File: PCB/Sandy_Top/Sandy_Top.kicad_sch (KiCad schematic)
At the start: 71 parts, among them J1 Conn_02x02_Top_Bottom, J2 Conn_02x02_Top_Bottom, J3 Conn_02x02_Top_Bottom

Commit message: WIP ネジ穴位置、スイッチ位置調整中
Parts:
- added H10, H9: MountingHole, locallib:MountingHole_2.2mm_M2_Pad_minimal, symbol Mechanical:MountingHole_Pad
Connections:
- net Top_GND: now also H10.1, H9.1
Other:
- note added: "Mid to Top: require 12 pins ( = 4 row + 7 col + GND )"
- note added: "ネジ穴をあと2本増やして12本にすれば、ネジ穴導通できる。"
- note removed: "Mid to Top: require 12 pins"
- moved on the sheet: H1, H2, H5, H6, H7, H8

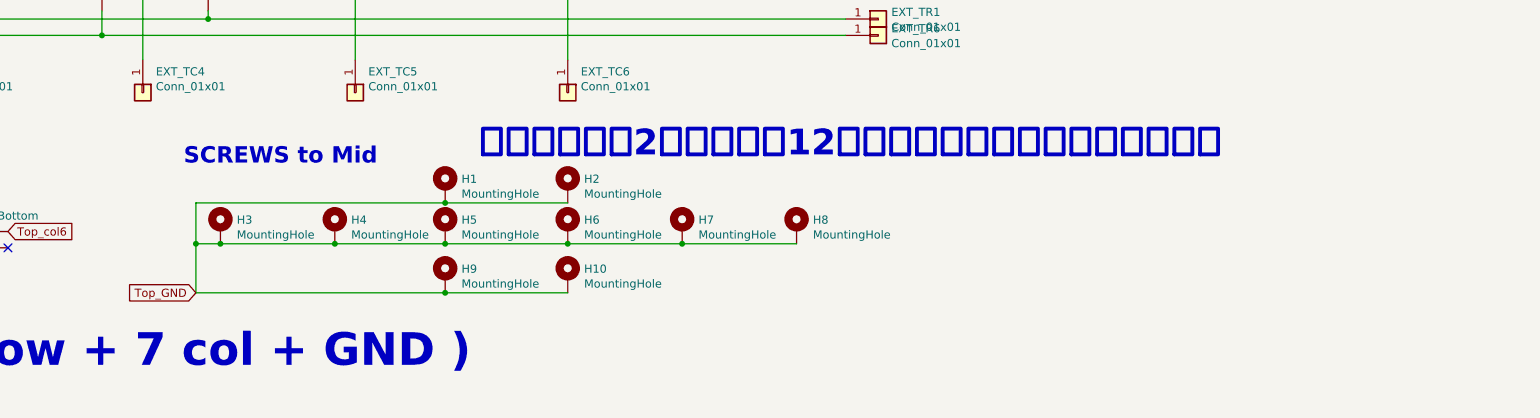
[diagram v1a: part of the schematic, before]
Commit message: Topネジ穴を仮配置
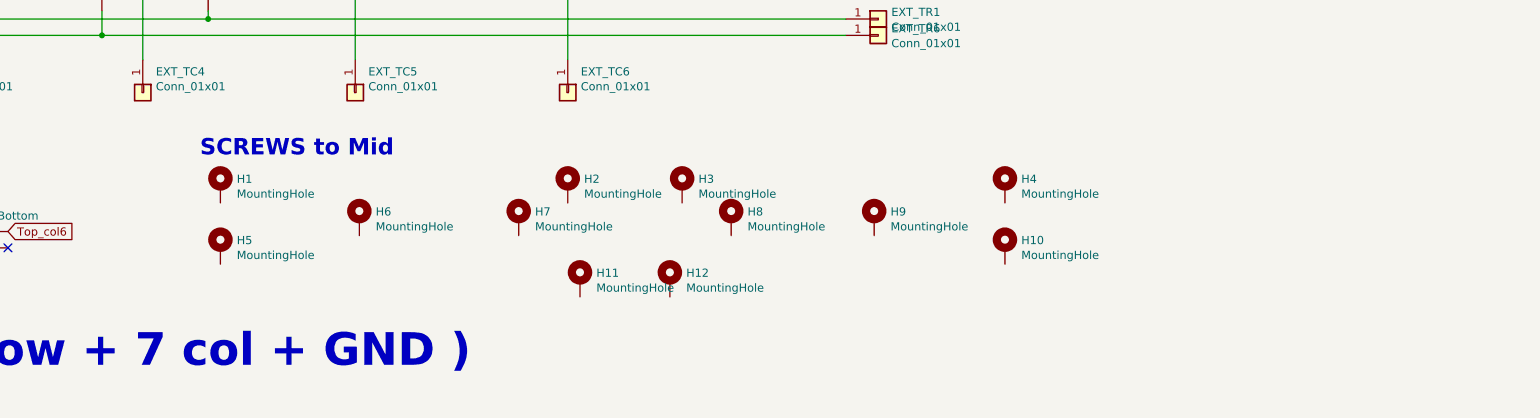
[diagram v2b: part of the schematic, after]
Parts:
- added H11, H12: MountingHole, locallib:MountingHole_2.2mm_M2_Pad_minimal, symbol Mechanical:MountingHole_Pad
- SW_4, SW_INS1: footprint MX_Alps_Hybrid:MXOnly-1U-Hotswap-guide -> MX_Alps_Hybrid:MXOnly-1U-Hotswap-screw-hole-side1-guide
- SW_5: footprint MX_Alps_Hybrid:MXOnly-1U-Hotswap-screw-hole-side2-guide -> MX_Alps_Hybrid:MXOnly-1U-Hotswap-guide
- SW_8: footprint MX_Alps_Hybrid:MXOnly-1U-Hotswap-screw-hole-side3-guide -> MX_Alps_Hybrid:MXOnly-1U-Hotswap-guide
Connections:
- net Top_GND: no longer H1.1, H10.1, H2.1, H3.1, H4.1, H5.1, H6.1, H7.1, H8.1, H9.1
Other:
- note removed: "ネジ穴をあと2本増やして12本にすれば、ネジ穴導通できる。"
- moved on the sheet: H1, H10, H3, H4, H5, H6, H7, H8, H9
